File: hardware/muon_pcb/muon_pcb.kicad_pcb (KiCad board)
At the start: 4 copper layers, 88 x 94.5 mm, 75 parts, among them J1 Conn_Coaxial, J12 USB_B_Micro, J2 Conn_Coaxial, J3 Conn_02x02_Top_Bottom, J4 Micro_SD_Card_Det1, J5 Conn_01x04, J6 Conn_01x02, J7 Conn_01x04, J8 Conn_02x06_Odd_Even, J9 SWD Port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

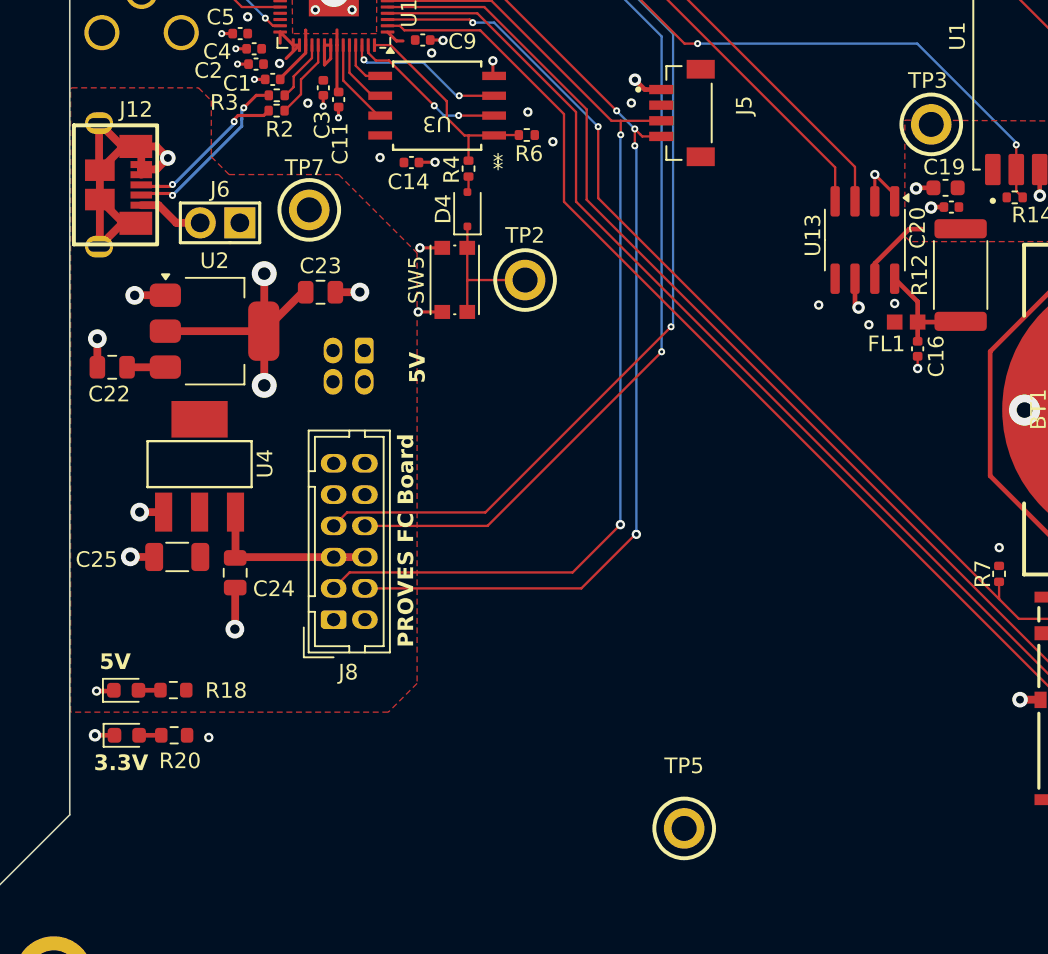
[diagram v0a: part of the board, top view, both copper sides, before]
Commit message: minor changes to layout & generated bom and gerber files
slightly altered usb trace impedance
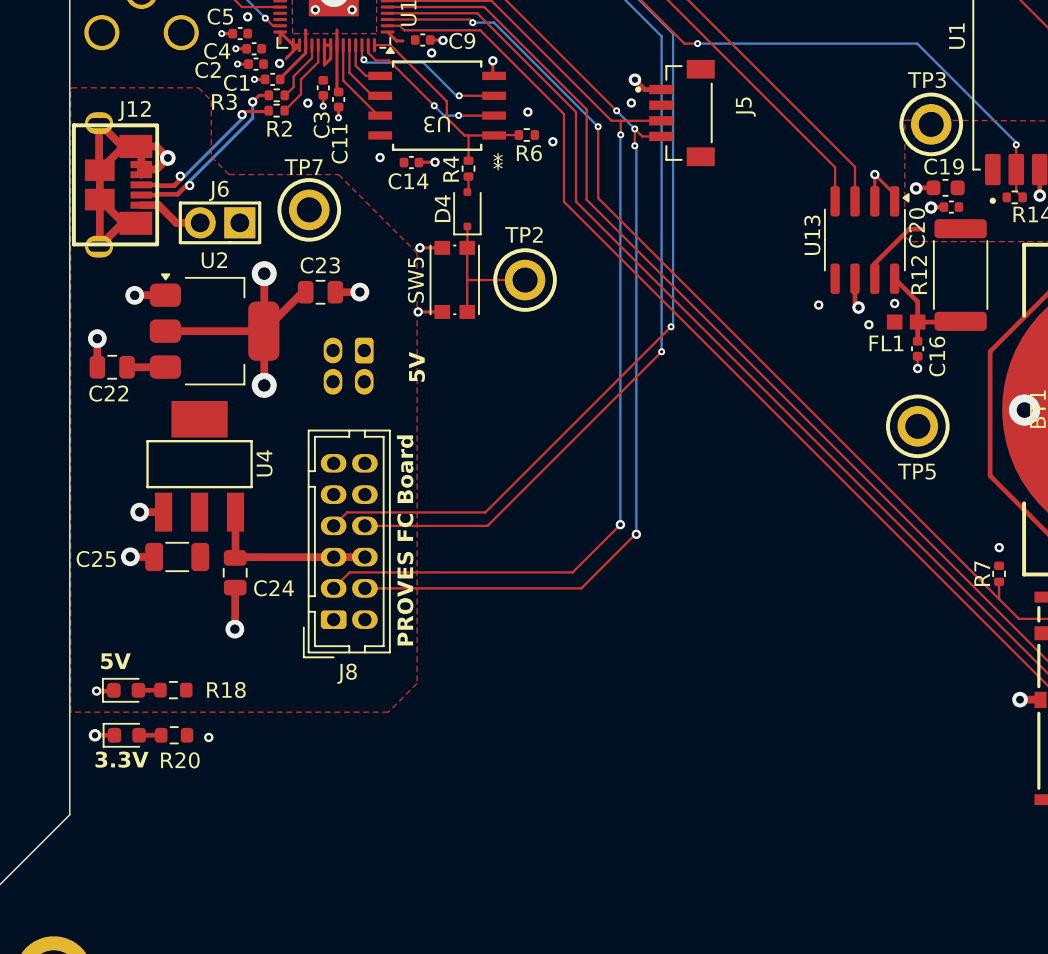
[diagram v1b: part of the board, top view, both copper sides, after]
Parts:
- moved TP5 29.8 mm to (151.8, 108.5)
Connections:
- U4 pad 4: (no net) -> +5V

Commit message: final changes?
maybe. pls be final for demo version
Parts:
- added J10: Conn_01x04, 1my_footprints:JST_BM04B-SRSS-TB(LF)(SN), F.Cu at (114.6, 95.2)
- C12, C13: footprint Capacitor_SMD:C_0201_0603Metric -> Capacitor_SMD:C_0402_1005Metric
- D2: footprint LED_SMD:LED_0201_0603Metric -> LED_SMD:LED_0402_1005Metric
- moved TP7 28.4 mm to (101.6, 120.7)
- moved C23 4.76 mm to (110.4, 103.5), turned to -90 degrees
- moved C22 3.82 mm to (100.4, 108.6), turned to -90 degrees
- moved U2 2.52 mm to (104.3, 101.8)
- moved C6 1.12 mm to (109.3, 79.0)
- moved J6 1.03 mm to (107.0, 96.5)
- moved J3 0.68 mm to (116.8, 104.2)
- moved D2 0.18 mm to (168.0, 93.9)
- moved C13 0.13 mm to (113.4, 72.3)
- moved C12 0.12 mm to (115.5, 70.5)
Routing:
- net USB_D+: track 10.4 -> 24.7 mm
- net USB_D-: track 11.6 -> 24.6 mm
- net +5V: track 2.45 -> 5.95 mm
- net GND: track 92.2 -> 90.1 mm, vias 66 -> 67
- net PAYLOAD_PWR: track 28.8 -> 27.8 mm
- net GPS 1PPS: track 87.2 -> 86.3 mm
- net Cosmic Analog: vias 1 -> 0

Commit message: added 3d models
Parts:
- R20: value 100k -> 6.8k
- moved J8 10.1 mm to (116.4, 111.0), turned to -90 degrees
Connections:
- J8 pad 1: GND -> PAYLOAD_PWR
- J8 pad 10: GND -> SDA0
- J8 pad 11: PAYLOAD_PWR -> GND
- J8 pad 12: PAYLOAD_PWR -> GND
- J8 pad 2: GND -> PAYLOAD_PWR
- J8 pad 3: SDA0 -> GND
- J8 pad 4: SCL0 -> GND
- J8 pad 5: PAYLOAD_BATT -> UART0 Tx
- J8 pad 6: PAYLOAD_BATT -> UART0 Rx
- J8 pad 7: UART0 Rx -> PAYLOAD_BATT
- J8 pad 8: UART0 Tx -> PAYLOAD_BATT
- J8 pad 9: GND -> SCL0
- U4 pad 4: +5V -> (no net)

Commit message: v1 firmware reference and beginning v2
uploaded cygnet devboard v1 firmware reference & updated schematic and layout for v2 demo. to do: assign new jlc part numbers
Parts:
- removed U15: TMP1075DSG, Package_SON:WSON-8-1EP_2x2mm_P0.5mm_EP0.9x1.6mm_ThermalVias
- added U5: TMP117xxDRV, Package_SON:WSON-6-1EP_2x2mm_P0.65mm_EP1x1.6mm, F.Cu at (138.7, 74.7)
- C17: value 10nF -> 100nF
- moved C17 25.0 mm to (138.7, 49.5)
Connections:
- U4 pad 4: (no net) -> +5V
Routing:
- net GND: track 90.1 -> 87.0 mm, vias 67 -> 66
- net SCL1: track 50.6 -> 52.5 mm
- net SDA1: track 51.6 -> 53.5 mm

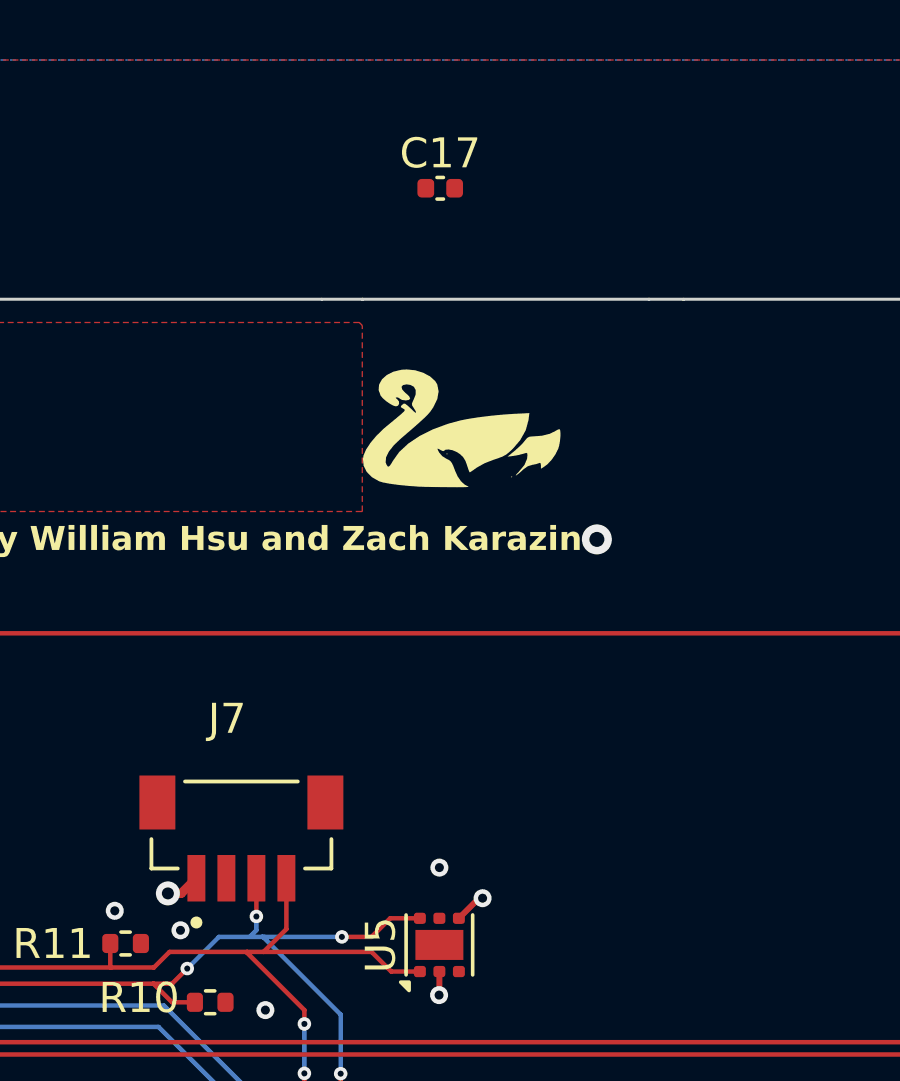
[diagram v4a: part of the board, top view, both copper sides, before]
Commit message: CADENCE Cygnet V2 (keeping same GPS)
Uses CD-PA1616D from Adafruit
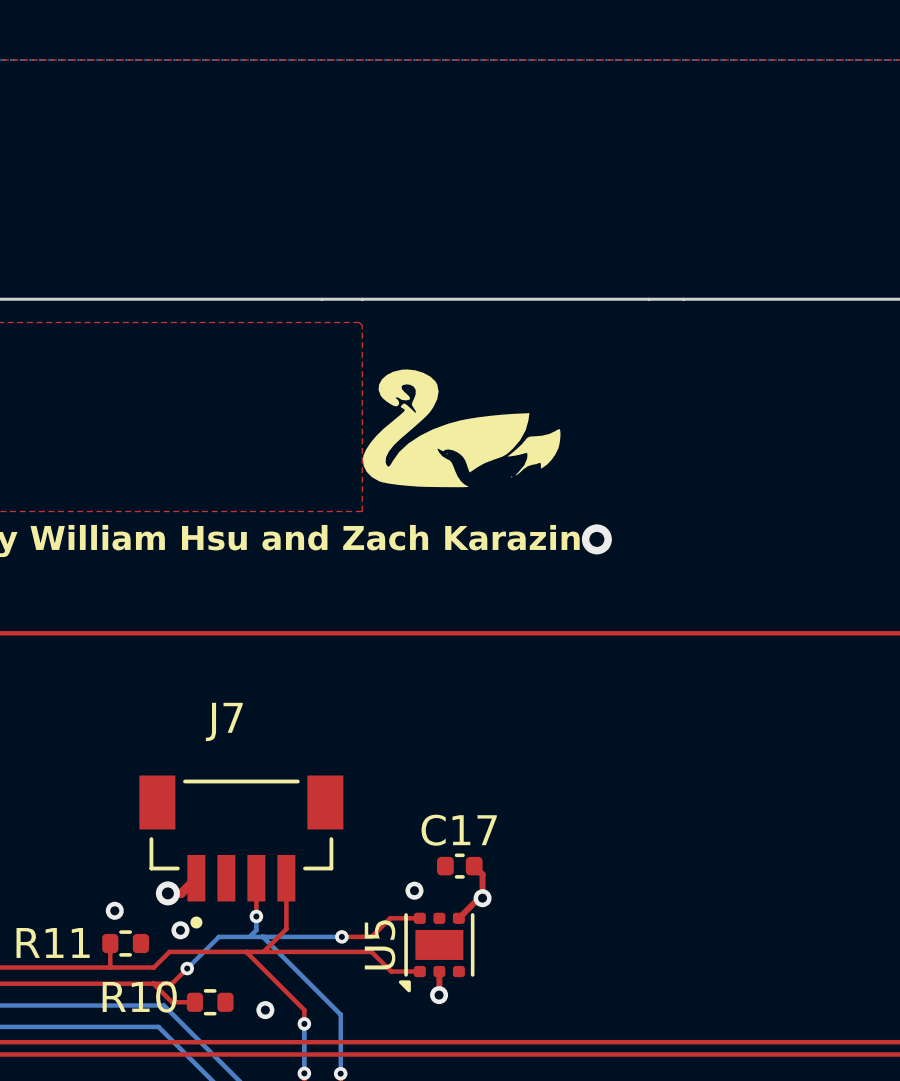
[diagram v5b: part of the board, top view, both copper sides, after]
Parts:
- moved C17 22.6 mm to (139.3, 72.1)
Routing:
- net GND: track 87.0 -> 88.2 mm
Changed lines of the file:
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@@
 			)
 		)
-		(property "LCSC" "C14675"
+		(property "LCSC" "C23212"
 			(at 0 0 0)
 			(layer "F.SilkS")
@@
 			)
 		)
+		(property "LCSC" "C699536"
+			(at 0 0 0)
+			(layer "F.SilkS")
+			(hide yes)
+			(effects
+				(font
+					(size 1.27 1.27)
+					(thickness 0.15)
+				)
+			)
+		)
 		(property ki_fp_filters "WSON*1EP?2x2mm?P0.65mm?EP1x1.6mm*")
 		(sheetname "/Sensors/")
@@
 	(footprint "Capacitor_SMD:C_0402_1005Metric"
 		(layer "F.Cu")
-		(at 138.6875 49.515)
+		(at 139.34 72.11)
 		(descr "Capacitor SMD 0402 (1005 Metric), square (rectangular) end terminal, IPC_7351 nominal, (Body size source: IPC-SM-782 page 76, https://www.pcb-3d.com/wordpress/wp-content/uploads/ipc-sm-782a_amendment_1_and_2.pdf), generated with kicad-footprint-generator")
 		(tags "capacitor")
@@
 			)
 		)
+		(property "LCSC" "C1525"
+			(at 0 0 0)
+			(layer "F.SilkS")
+			(hide yes)
+			(effects
+				(font
+					(size 1.27 1.27)
+					(thickness 0.15)
+				)
+			)
+		)
 		(property ki_fp_filters "C_*")
 		(sheetname "/Sensors/")
@@
 	)
 	(segment
+		(start 140.1 73.18)
+		(end 140.1 72.39)
+		(width 0.2)
+		(layer "F.Cu")
+		(net 5)
+	)
+	(segment
 		(start 99.45 94.01)
 		(end 99.45 96.97)
@@
 	)
 	(segment
+		(start 140.1 72.39)
+		(end 139.82 72.11)
+		(width 0.2)
+		(layer "F.Cu")
+		(net 5)
+	)
+	(segment
 		(start 168.5 93.95)
 		(end 168.5 94.7)
@@
 	)
 	(via
-		(at 138.66 72.16)
+		(at 137.83 72.93)
 		(size 0.6)
 		(drill 0.3)
